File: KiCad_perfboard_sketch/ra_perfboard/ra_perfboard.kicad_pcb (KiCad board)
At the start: 2 copper layers, 71.1 x 66 mm, 1 part

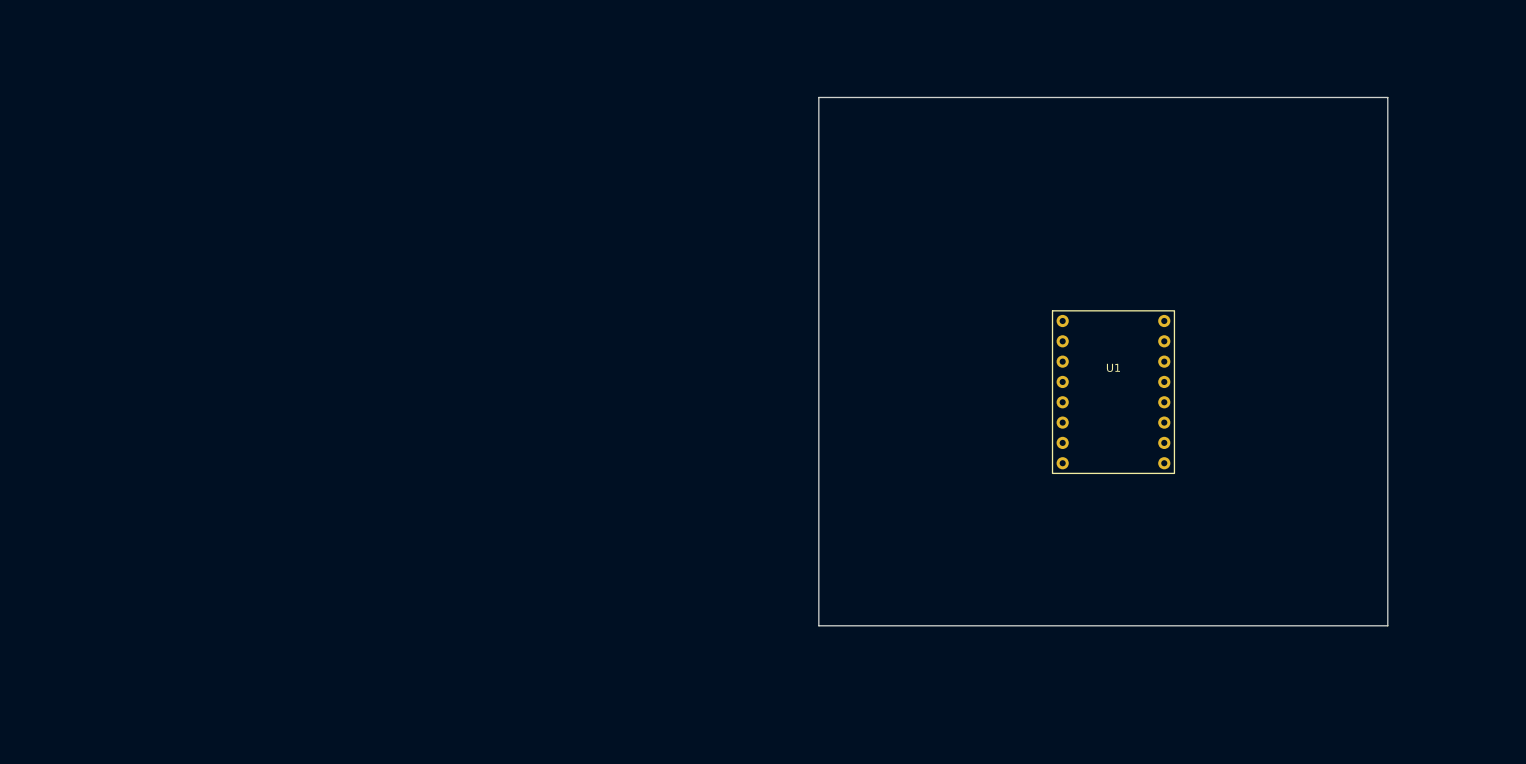
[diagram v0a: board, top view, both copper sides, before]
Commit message: Added STM32 board symbol and footprint.
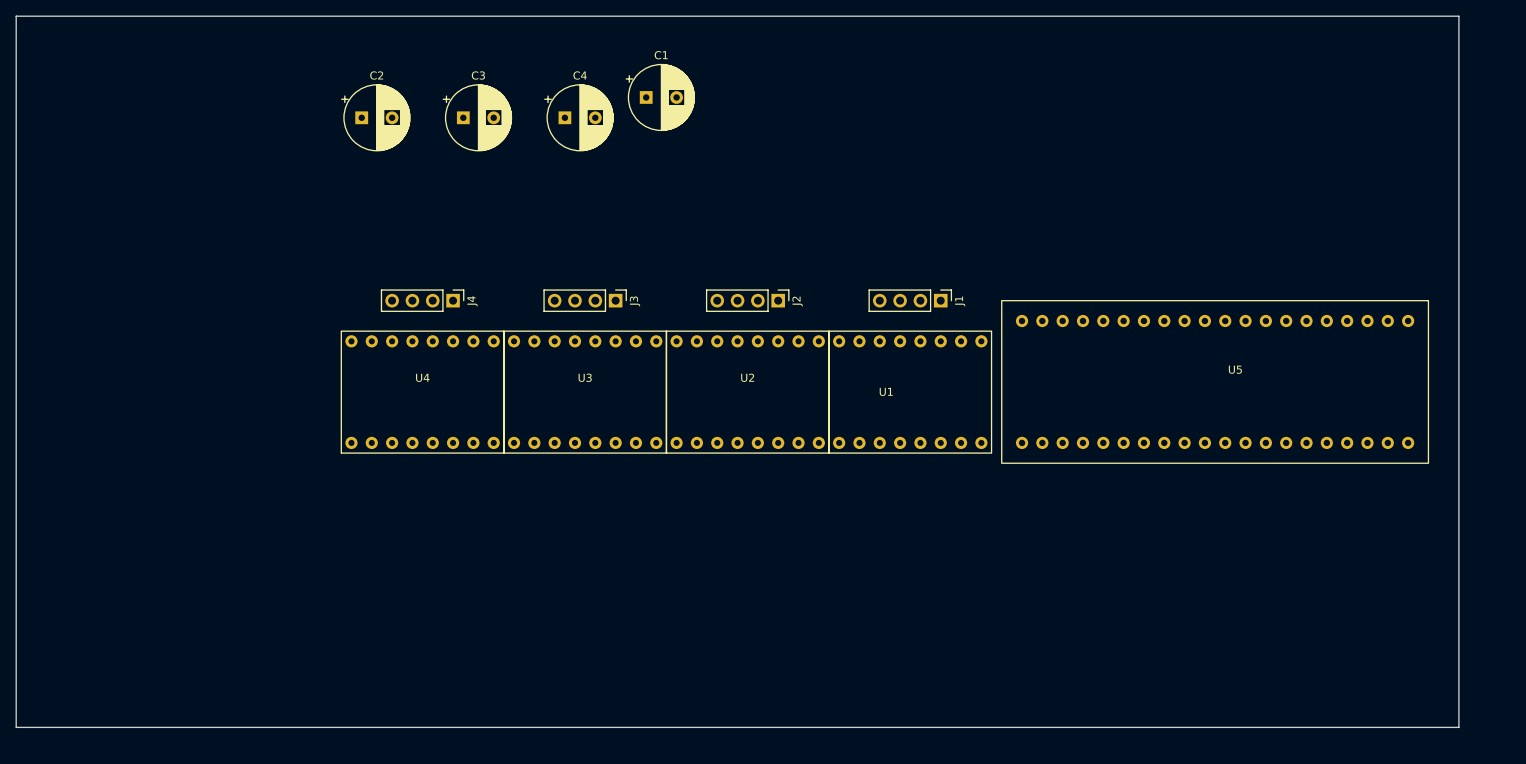
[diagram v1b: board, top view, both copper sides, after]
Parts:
- added C1: M1_Cap, Capacitor_THT:CP_Radial_D8.0mm_P3.80mm, F.Cu at (110.5, 58.4)
- added C2: M2_Cap, Capacitor_THT:CP_Radial_D8.0mm_P3.80mm, F.Cu at (74.9, 61.0)
- added C3: M3_Cap, Capacitor_THT:CP_Radial_D8.0mm_P3.80mm, F.Cu at (87.6, 61.0)
- added C4: M4_Cap, Capacitor_THT:CP_Radial_D8.0mm_P3.80mm, F.Cu at (100.3, 61.0)
- added J1: M1, Connector_PinHeader_2.54mm:PinHeader_1x04_P2.54mm_Vertical, F.Cu at (147.3, 83.8)
- added J2: M2, Connector_PinHeader_2.54mm:PinHeader_1x04_P2.54mm_Vertical, F.Cu at (127.0, 83.8)
- added J3: M3, Connector_PinHeader_2.54mm:PinHeader_1x04_P2.54mm_Vertical, F.Cu at (106.7, 83.8)
- added J4: M4, Connector_PinHeader_2.54mm:PinHeader_1x04_P2.54mm_Vertical, F.Cu at (86.4, 83.8)
- added U2: ~, stm32_ra_board_footprints:TMC2208_Board_Footprint, F.Cu at (123.2, 95.2)
- added U3: ~, stm32_ra_board_footprints:TMC2208_Board_Footprint, F.Cu at (102.9, 95.2)
- added U4: ~, stm32_ra_board_footprints:TMC2208_Board_Footprint, F.Cu at (82.5, 95.2)
- added U5: STM32F411CEU6_Board, stm32_ra_board_footprints:STM32F411CEU6_Board, F.Cu at (181.6, 94.0)
- moved U1 25.4 mm to (143.5, 95.2), turned to 90 degrees
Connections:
- U1 pad 1: unconnected-(U1-EN-Pad1) -> /M1_EN
- U1 pad 10: unconnected-(U1-VIO-Pad10) -> +3V3
- U1 pad 11: unconnected-(U1-1B-Pad11) -> Net-(J1-Pin_1)
- U1 pad 12: unconnected-(U1-1A-Pad12) -> Net-(J1-Pin_2)
- U1 pad 13: unconnected-(U1-2A-Pad13) -> Net-(J1-Pin_3)
- U1 pad 14: unconnected-(U1-2B-Pad14) -> Net-(J1-Pin_4)
- U1 pad 15: unconnected-(U1-GND-Pad15) -> GND
- U1 pad 16: unconnected-(U1-+VMOT-Pad16) -> +24V
- U1 pad 2: unconnected-(U1-MS1-Pad2) -> +3V3
- U1 pad 3: unconnected-(U1-MS2-Pad3) -> +3V3
- U1 pad 7: unconnected-(U1-STEP-Pad7) -> /M1_STEP
- U1 pad 8: unconnected-(U1-DIR-Pad8) -> /M1_DIR
- U1 pad 9: unconnected-(U1-GND-Pad9) -> GND
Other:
- board size 71.1 x 66 mm -> 180.3 x 88.9 mm

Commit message: Added TCA9548A and LM3596 boards to perfboard layout.
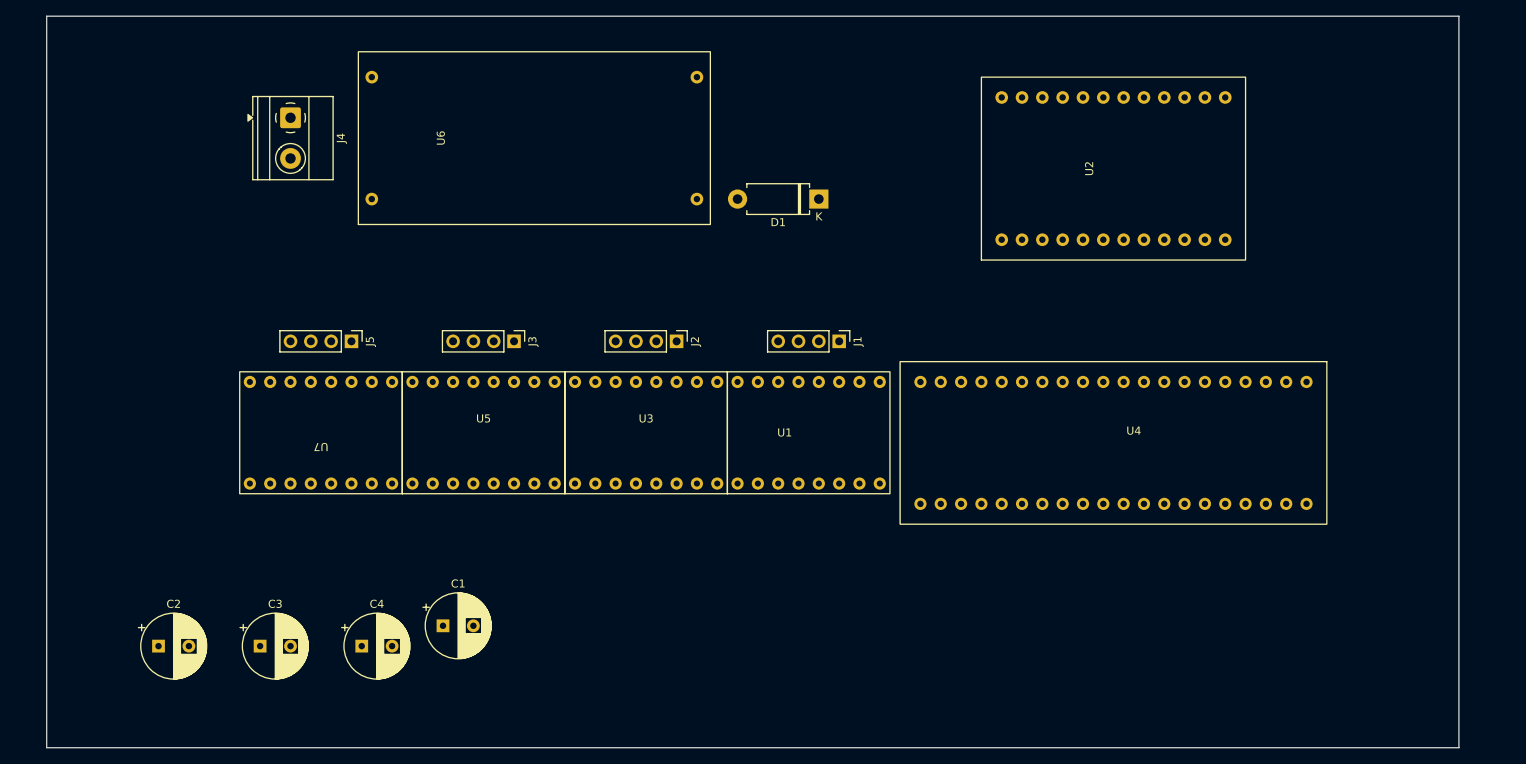
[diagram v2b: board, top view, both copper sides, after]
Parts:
- added D1: D, Diode_THT:D_DO-15_P10.16mm_Horizontal, F.Cu at (132.1, 71.1)
- added J4: Terminal, TerminalBlock_Phoenix:TerminalBlock_Phoenix_MKDS-1,5-2-5.08_1x02_P5.08mm_Horizontal, F.Cu at (66.0, 61.0)
- added U2: TCA9548A_Board, stm32_ra_board_footprints:TCA9548A_Board_Footprint, F.Cu at (168.9, 67.3)
- added U6: ~, stm32_ra_board_footprints:LM2596_Board_BC_Footprint, F.Cu at (96.5, 63.5)
- moved C1 70.8 mm to (85.1, 124.5)
- moved C2 70.8 mm to (49.5, 127.0)
- moved C3 70.8 mm to (62.2, 127.0)
- moved C4 70.8 mm to (74.9, 127.0)
- moved U4 14.8 mm to (168.9, 101.6)
- moved J2 13.7 mm to (114.3, 88.9)
- moved J3 13.7 mm to (94.0, 88.9)
- moved J5 13.7 mm to (73.7, 88.9)
- moved U3 13.7 mm to (110.5, 100.3)
- moved U5 13.7 mm to (90.2, 100.3)
- moved U7 13.7 mm to (69.8, 100.3), turned to -90 degrees
- moved J1 13.7 mm to (134.6, 88.9)
- moved U1 13.7 mm to (130.8, 100.3)
- renumbered J4 to J5, U2 to U3, U5 to U4, U3 to U5, U4 to U7
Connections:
- C1 pad 1: GND -> +24V
- C1 pad 2: +24V -> GND
- C2 pad 1: GND -> unconnected-(C2-Pad1)
- C2 pad 2: +24V -> GND
- C3 pad 1: GND -> +24V
- C3 pad 2: +24V -> GND
- C4 pad 1: GND -> +24V
- C4 pad 2: +24V -> GND
- U4 pad 19: unconnected-(U5-G-Pad19) -> GND
- U4 pad 22: unconnected-(U5-G-Pad22) -> GND
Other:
- board size 180.3 x 88.9 mm -> 176.5 x 91.4 mm

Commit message: Configured pins in .ioc file and worked on KiCad perfboard.
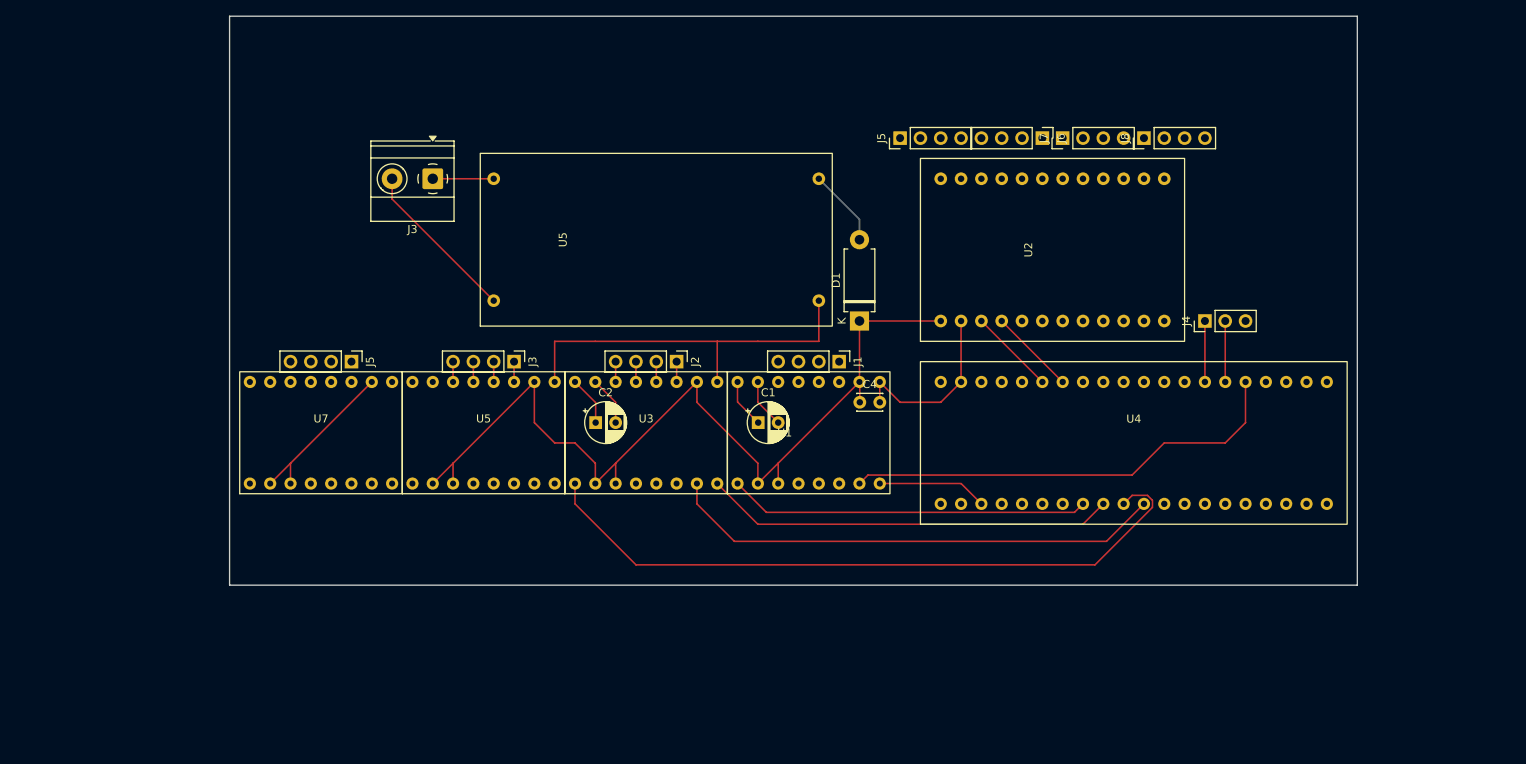
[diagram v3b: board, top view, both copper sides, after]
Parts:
- removed C3: M3_Cap, Capacitor_THT:CP_Radial_D8.0mm_P3.80mm
- added J4: USART, Connector_PinHeader_2.54mm:PinHeader_1x03_P2.54mm_Vertical, F.Cu at (180.3, 86.4)
- added J5: ~, Connector_PinHeader_2.54mm:PinHeader_1x04_P2.54mm_Vertical, F.Cu at (142.2, 63.5)
- added J6: ~, Connector_PinHeader_2.54mm:PinHeader_1x04_P2.54mm_Vertical, F.Cu at (160.0, 63.5)
- added J7: ~, Connector_PinHeader_2.54mm:PinHeader_1x04_P2.54mm_Vertical, F.Cu at (162.6, 63.5)
- added J8: ~, Connector_PinHeader_2.54mm:PinHeader_1x04_P2.54mm_Vertical, F.Cu at (172.7, 63.5)
- C1, C2: footprint Capacitor_THT:CP_Radial_D8.0mm_P3.80mm -> Capacitor_THT:CP_Radial_D5.0mm_P2.50mm
- C4: value M4_Cap -> 100nF; footprint Capacitor_THT:CP_Radial_D8.0mm_P3.80mm -> Capacitor_THT:C_Disc_D3.0mm_W2.0mm_P2.50mm
- moved C4 69.3 mm to (137.2, 96.5)
- moved C2 61.4 mm to (104.2, 99.1)
- moved C1 46.9 mm to (124.5, 99.1)
- moved U5 19.8 mm to (111.8, 76.2)
- moved J3 19.3 mm to (83.8, 68.6), turned to 180 degrees
- moved D1 16.1 mm to (137.2, 86.4), turned to 90 degrees
- moved U2 12.7 mm to (161.3, 77.5)
- moved J1 2.54 mm to (134.6, 91.4)
- moved J2 2.54 mm to (114.3, 91.4)
- moved J3 2.54 mm to (94.0, 91.4)
- moved J5 2.54 mm to (73.7, 91.4)
- moved U4 2.54 mm to (171.4, 101.6), turned to 90 degrees
- turned U7 to 90 degrees
- renumbered J4 to J3, U6 to U5
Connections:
- C2 pad 1: unconnected-(C2-Pad1) -> +24V
- C4 pad 1: +24V -> +3V3
- U2 pad 3: unconnected-(U2-SDA-Pad3) -> /I2C1_SDA
- U2 pad 4: unconnected-(U2-SCL-Pad4) -> /I2C1_SCL
- U4 pad 10: unconnected-(U4-PA4-Pad10) -> /M2_EN
- U4 pad 11: unconnected-(U4-PA5-Pad11) -> /M2_STEP
- U4 pad 26: unconnected-(U4-PB7-Pad26) -> /I2C1_SDA
- U4 pad 27: unconnected-(U4-PB6-Pad27) -> /I2C1_SCL
- U4 pad 3: unconnected-(U4-PC14-Pad3) -> /M1_DIR
- U4 pad 34: unconnected-(U4-PA10-Pad34) -> /USART1_RX
- U4 pad 35: unconnected-(U4-PA9-Pad35) -> /USART1_TX
- U4 pad 36: unconnected-(U4-PA8-Pad36) -> /M1_STEP
- U4 pad 8: unconnected-(U4-PA2-Pad8) -> /M1_EN
- U4 pad 9: unconnected-(U4-PA3-Pad9) -> /M2_DIR
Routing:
- net +3V3: track 0.00 -> 135.5 mm
- net GND: track 0.00 -> 103.4 mm
- net /M2_EN: track 0.00 -> 86.0 mm
- net /M2_STEP: track 0.00 -> 62.3 mm
- net /M1_STEP: track 0.00 -> 56.5 mm
- net /M2_DIR: track 0.00 -> 51.4 mm
- net /M1_EN: track 0.00 -> 45.1 mm
- net +24V: track 0.00 -> 19.9 mm
- net /M1_DIR: track 0.00 -> 13.8 mm
- net /I2C1_SDA: track 0.00 -> 10.8 mm
- net /I2C1_SCL: track 0.00 -> 10.8 mm
- net Net-(D1-A): track 0.00 -> 9.72 mm
- net /USART1_RX: track 0.00 -> 7.62 mm
- net /USART1_TX: track 0.00 -> 7.22 mm
- net Net-(J3-Pin_4): track 0.00 -> 2.54 mm
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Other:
- board size 176.5 x 91.4 mm -> 141 x 71.1 mm

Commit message: Updated commands to be use 2 bytes instead of 1, and made modifications on perfboard and pins.
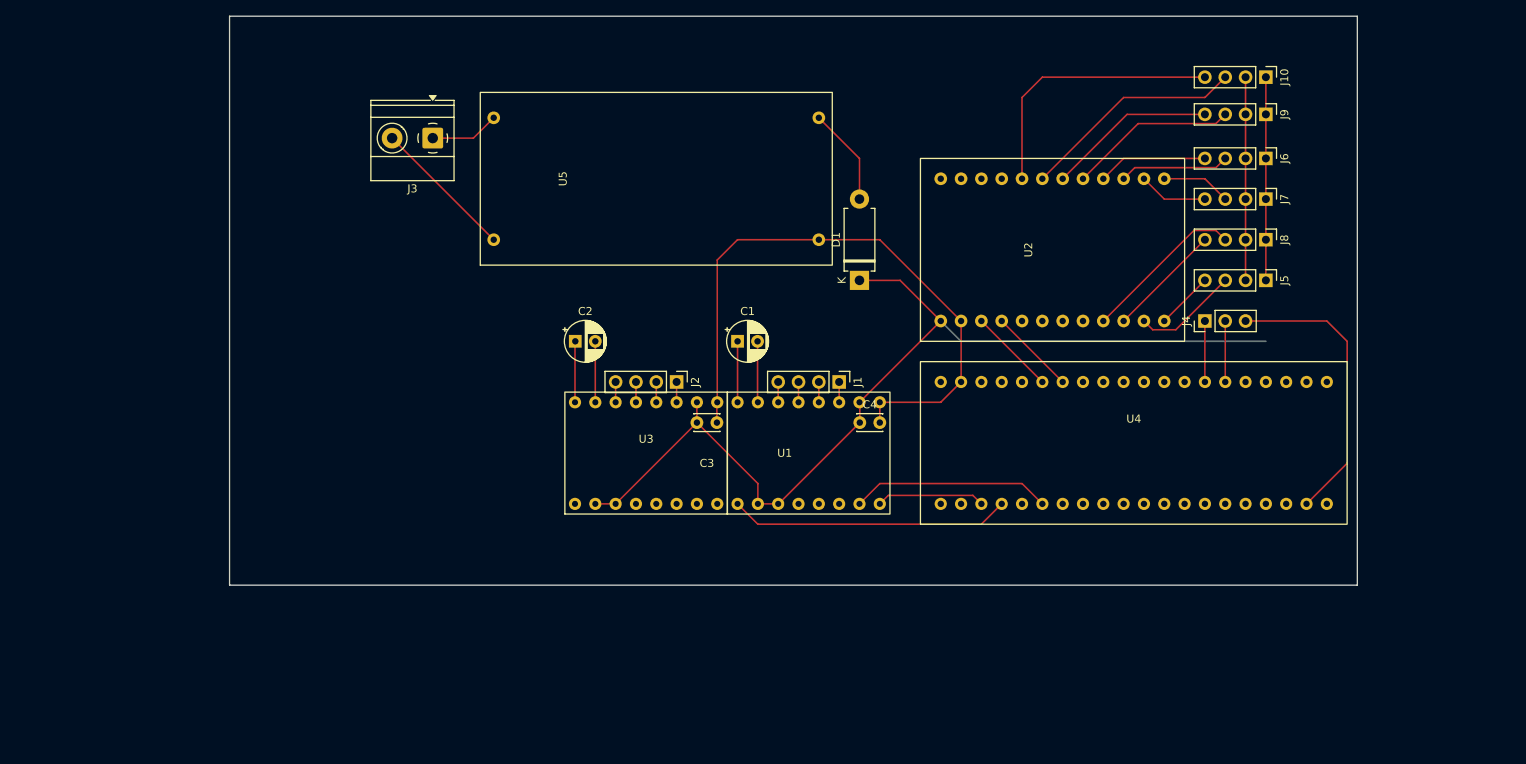
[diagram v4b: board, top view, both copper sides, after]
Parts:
- removed the J3 at (94.0, 91.4)
- removed the J5 at (73.7, 91.4)
- removed the U5 at (90.2, 100.3)
- removed U7: ~, stm32_ra_board_footprints:TMC2208_Board_Footprint
- added C3: 100nF, Capacitor_THT:C_Disc_D3.0mm_W2.0mm_P2.50mm, F.Cu at (116.8, 99.1)
- added J10: L6, Connector_PinHeader_2.54mm:PinHeader_1x04_P2.54mm_Vertical, F.Cu at (188.0, 55.9)
- added J9: L5, Connector_PinHeader_2.54mm:PinHeader_1x04_P2.54mm_Vertical, F.Cu at (188.0, 60.5)
- J5: value ~ -> L3
- J6: value ~ -> L1
- J7: value ~ -> L2
- J8: value ~ -> L4
- moved J5 49.1 mm to (188.0, 81.3), turned to -90 degrees
- moved J6 28.1 mm to (188.0, 66.0)
- moved J7 26.5 mm to (188.0, 71.1), turned to -90 degrees
- moved J8 19.8 mm to (188.0, 76.2), turned to -90 degrees
- moved C1 10.5 mm to (121.9, 88.9)
- moved C2 10.5 mm to (101.6, 88.9)
- moved U5 7.62 mm to (111.8, 68.6)
- moved D1 5.08 mm to (137.2, 81.3)
- moved J3 5.08 mm to (83.8, 63.5)
- moved C4 2.54 mm to (137.2, 99.1)
- moved J1 2.54 mm to (134.6, 94.0)
- moved J2 2.54 mm to (114.3, 94.0)
- moved U1 2.54 mm to (130.8, 102.9)
- moved U3 2.54 mm to (110.5, 102.9)
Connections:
- J5 pad 1: unconnected-(J5-Pin_1-Pad1) -> +3V3
- J5 pad 2: unconnected-(J5-Pin_2-Pad2) -> GND
- J5 pad 3: unconnected-(J5-Pin_3-Pad3) -> /SDA1
- J5 pad 4: unconnected-(J5-Pin_4-Pad4) -> /SCL1
- J6 pad 1: unconnected-(J6-Pin_1-Pad1) -> +3V3
- J6 pad 2: unconnected-(J6-Pin_2-Pad2) -> GND
- J6 pad 3: unconnected-(J6-Pin_3-Pad3) -> /SDA3
- J6 pad 4: unconnected-(J6-Pin_4-Pad4) -> /SCL3
- J7 pad 1: unconnected-(J7-Pin_1-Pad1) -> +3V3
- J7 pad 2: unconnected-(J7-Pin_2-Pad2) -> GND
- J7 pad 3: unconnected-(J7-Pin_3-Pad3) -> /SDA2
- J7 pad 4: unconnected-(J7-Pin_4-Pad4) -> /SCL2
- J8 pad 1: unconnected-(J8-Pin_1-Pad1) -> +3V3
- J8 pad 2: unconnected-(J8-Pin_2-Pad2) -> GND
- J8 pad 3: unconnected-(J8-Pin_3-Pad3) -> /SDA0
- J8 pad 4: unconnected-(J8-Pin_4-Pad4) -> /SCL0
- U2 pad 10: unconnected-(U2-SC0-Pad10) -> /SCL0
- U2 pad 11: unconnected-(U2-SD1-Pad11) -> /SDA1
- U2 pad 12: unconnected-(U2-SC1-Pad12) -> /SCL1
- U2 pad 17: unconnected-(U2-SC5-Pad17) -> /SCL5
- U2 pad 18: unconnected-(U2-SD5-Pad18) -> /SDA5
- U2 pad 19: unconnected-(U2-SC4-Pad19) -> /SCL4
- U2 pad 20: unconnected-(U2-SD4-Pad20) -> /SDA4
- U2 pad 21: unconnected-(U2-SC3-Pad21) -> /SCL3
- U2 pad 22: unconnected-(U2-SD3-Pad22) -> /SDA3
- U2 pad 23: unconnected-(U2-SC2-Pad23) -> /SCL2
- U2 pad 24: unconnected-(U2-SD2-Pad24) -> /SDA2
- U2 pad 9: unconnected-(U2-SD0-Pad9) -> /SDA0
- U4 pad 36: /M1_STEP -> unconnected-(U4-PA8-Pad36)
- U4 pad 4: unconnected-(U4-PC15-Pad4) -> /M1_EN
- U4 pad 6: unconnected-(U4-PA0-Pad6) -> /M1_STEP
- U4 pad 8: /M1_EN -> unconnected-(U4-PA2-Pad8)
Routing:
- net /M2_EN: track 86.0 -> 0.00 mm
- net GND: track 103.4 -> 172.2 mm
- net /M2_STEP: track 62.3 -> 0.00 mm
- net /M2_DIR: track 51.4 -> 0.00 mm
- net /SCL5: track 0.00 -> 34.1 mm
- net /M1_STEP: track 56.5 -> 25.0 mm
- net /SDA5: track 0.00 -> 28.1 mm
- net /SDA4: track 0.00 -> 21.1 mm
- net /SCL4: track 0.00 -> 21.1 mm
- net /SDA0: track 0.00 -> 20.4 mm
- net /SCL0: track 0.00 -> 14.4 mm
- net /SCL3: track 0.00 -> 13.8 mm
- net /SDA3: track 0.00 -> 13.8 mm
- net /SDA1: track 0.00 -> 13.2 mm
- net +3V3: track 135.5 -> 146.0 mm
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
